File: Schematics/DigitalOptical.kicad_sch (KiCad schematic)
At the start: 112 parts, among them Q1 BSS138, Q2 BSS138, Q3 BSS138, Q4 BSS138, Q5 BSS138, Q6 BSS138, U100 PC817, U63 PC817, U64 PC817, U65 PCF8575, U66 PC817, U67 PC817, U68 PC817, U69 PC817, U70 PC817, U71 PC817, U72 PC817, U73 PC817, U74 LM1117-3.3, U75 PC817, U76 PC817, U77 PCF8575, U78 PCF8575, U79 PC817, U80 PC817, U81 PC817, U82 PC817, U83 PC817, U84 PC817, U85 PC817, U86 PC817, U87 LM1117-3.3, U88 LM1117-3.3, U89 PC817, U90 PC817, U91 PC817, U92 PC817, U93 PC817, U94 PC817, U95 PC817, U96 PC817, U97 PC817, U98 PC817, U99 PC817

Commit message: Prelude to split configurations.
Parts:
- removed C83, C84: .1µF, symbol Device:C_Small
- removed JD1, JD10, JD11, JD13, JD14, JD15, JD16, JD17, JD18, JD19, JD2, JD20, JD21, JD3, JD4, JD5, JD7, JD8: From 12v Analog, symbol Connector_Generic:Conn_01x02
- removed JD12, JD6, JD9: Conn_01x03, symbol Connector_keyed_kicad_sym:Conn_01x03
- removed Q1, Q2: BSS138, digikey-footprints:SOT-23-3, symbol dk_Transistors-FETs-MOSFETs-Single:BSS138
- removed U100, U63, U64, U66, U67, U68, U69, U70, U71, U72, U73, U75, U76, U79, U80, U81, U82, U83, U84, U85, U86, U89, U90, U91, U92, U93, U94, U95, U96, U97, U98, U99: PC817, Package_DIP:DIP-4_W7.62mm, symbol Isolator:PC817
- removed U65: PCF8575, IPC7351-Nominal:SOP65P775X200-24, symbol NXP:PCF8575
- removed U74: LM1117-3.3, symbol Regulator_Linear:LM1117-3.3
- added C20, C21: .1µF, symbol Device:C_Small
- added C30: 10µF, symbol Device:C_Polarized_Small_US
- added JP5: From 12v Analog, symbol Connector_Generic:Conn_01x02
- added Q13, Q14: BSS138, digikey-footprints:SOT-23-3, symbol dk_Transistors-FETs-MOSFETs-Single:BSS138
- added R153, R154, R155, R156, R157, R158, R159, R160, R161, R162, R163, R164, R165, R166: 10k, symbol Device:R_Small_US
- added U11: PCF8575, IPC7351-Nominal:SOP65P775X200-24, symbol NXP:PCF8575
- added U7: LM1117-3.3, symbol Regulator_Linear:LM1117-3.3
- R100, R101, R102, R103, R104, R107, R108, R111, R112, R113, R114, R115, R116, R117, R118, R119, R120, R121, R122, R123, R124, R85, R86, R87, R88, R91, R92, R93, R94, R97, R98, R99: value 220 -> 10k
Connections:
- net GNDA: now also C85.2, C86.2, C87.2, C88.2, JS3.3 (Pin_3), JS3.6 (Pin_6), U77.12 (VSS), U77.2 (A1), U77.21 (A0), U77.3 (A2), U78.12 (VSS), U78.2 (A1), U78.3 (A2), U87.1 (GND), U88.1 (GND), C30.2, JP5.2 (Pin_2)
- net SCL0: now also Q13.3; no longer R90.1
- net SDA0: now also Q14.3; no longer R95.1
- net at R120.2: now also C87.1, Q4.1, Q6.1, R106.2, R107.1, R108.2, R110.2, R111.1, R112.2, R113.1, R114.2, R115.1, R116.2, R117.1, R118.2, R119.1, R121.1, R122.2, R123.1, R124.2, U78.21 (A0), U78.24 (VDD), U88.2 (VO)
- net at R86.2: now also C86.1, Q3.1, Q5.1, R100.2, R105.2, R109.2, R85.1, R87.1, R88.2, R89.1, R90.2, R91.1, R92.2, R93.1, R94.2, R95.1, R96.2, R97.1, R98.2, R99.1, U77.24 (VDD), U87.2 (VO)
- net at R118.1: now also U78.16 (P13); no longer U78.17 (P14)
- net at U77.18 (P15): now also R90.1; no longer R119.2
- net at U77.9 (P05): now also R95.2; no longer R99.2
- net at R120.1: now also U78.15 (P12); no longer U78.18 (P15)
- net at R101.1: now also R102.2, R103.1, R104.2, C21.1, Q13.1, Q14.1, R153.2, R154.2, R155.1, R156.2, R157.1, R158.2, R159.1, R160.2, R161.1, R162.2, R163.1, R164.2, R165.1, R166.2, U11.2 (A1), U11.24 (VDD), U7.2 (VO)
- net at U78.10 (P06): now also R121.2; no longer R102.1
- net at R114.1: now also U78.18 (P15); no longer U78.15 (P12)
- net at U78.11 (P07): now also R123.2; no longer R104.1
- net at U78.9 (P05): now also R119.2; no longer R100.1
- net at U78.5 (P01): now also R111.2; no longer R88.1
- net at U77.14 (P11): now also R98.1; no longer R111.2
- net at R97.2: now also U77.10 (P06); no longer U77.8 (P04)
- net at R89.2: now also U77.6 (P02); no longer R96.2
- net at R96.1: now also U77.15 (P12)
- net at R113.2: now also U78.6 (P02); no longer U77.15 (P12)
- net at R107.2: now also U78.4 (P00); no longer U77.13 (P10)
- net at U77.7 (P03): now also R91.2; no longer R93.2
- net at R124.1: now also U78.13 (P10); no longer U78.20 (P17)
- net at R122.1: now also U78.14 (P11); no longer U78.19 (P16)
- net at R92.1: now also U77.17 (P14); no longer U78.6 (P02)
- net at R103.2: now also U11.5 (P01); no longer U77.11 (P07)
- net at R108.1: now also U78.20 (P17); no longer U78.13 (P10)
- net at R101.2: now also U11.4 (P00); no longer U77.10 (P06)
- net at U77.16 (P13): now also R94.1; no longer R115.2
- net at R117.2: now also U78.8 (P04); no longer U77.17 (P14)
- net at U77.19 (P16): now also R88.1; no longer R121.2
- net at U77.20 (P17): now also R86.1; no longer R123.2
- net at R112.1: now also U78.19 (P16); no longer U78.14 (P11)
- net at R116.1: now also U78.17 (P14); no longer U78.16 (P13)
- net at U78.7 (P03): now also R115.2; no longer R94.1
- net +5VD renamed +5V
- net +5V: now also C20.1, C30.1, JP5.1 (Pin_1), U7.3 (VI); no longer JS3.1 (Pin_1), JS3.2 (Pin_2), R90.2, R95.2
- new net: C20.2, C21.2, U11.12 (VSS), U11.21 (A0), U11.3 (A2), U7.1 (GND)
- new net: R157.2, U11.7 (P03)
- new net: R155.2, U11.6 (P02)
- new net: R164.1, U11.14 (P11)
- new net: Q14.2, R154.1, U11.23 (SDA)
- new net: R100.1, U77.13 (P10)
- new net: R159.2, U11.8 (P04)
- new net: R163.2, U11.10 (P06)
- new net: R165.2, U11.11 (P07)
- new net: R99.2, U77.11 (P07)
- new net: R93.2, U77.8 (P04)
- new net: Q13.2, R153.1, U11.22 (SCL)
- new net: R104.1, U11.19 (P16)
- new net: R162.1, U11.15 (P12)
- new net: R166.1, U11.13 (P10)
- new net: JS3.1 (Pin_1), JS3.2 (Pin_2)
- new net: R156.1, U11.18 (P15)
- new net: R161.2, U11.9 (P05)
- new net: R158.1, U11.17 (P14)
- new net: R160.1, U11.16 (P13)
- new net: R102.1, U11.20 (P17)
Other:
- moved on the sheet: C85, C86, C87, C88, JS3, Q3, Q4, Q5, Q6, R105, R106, R109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

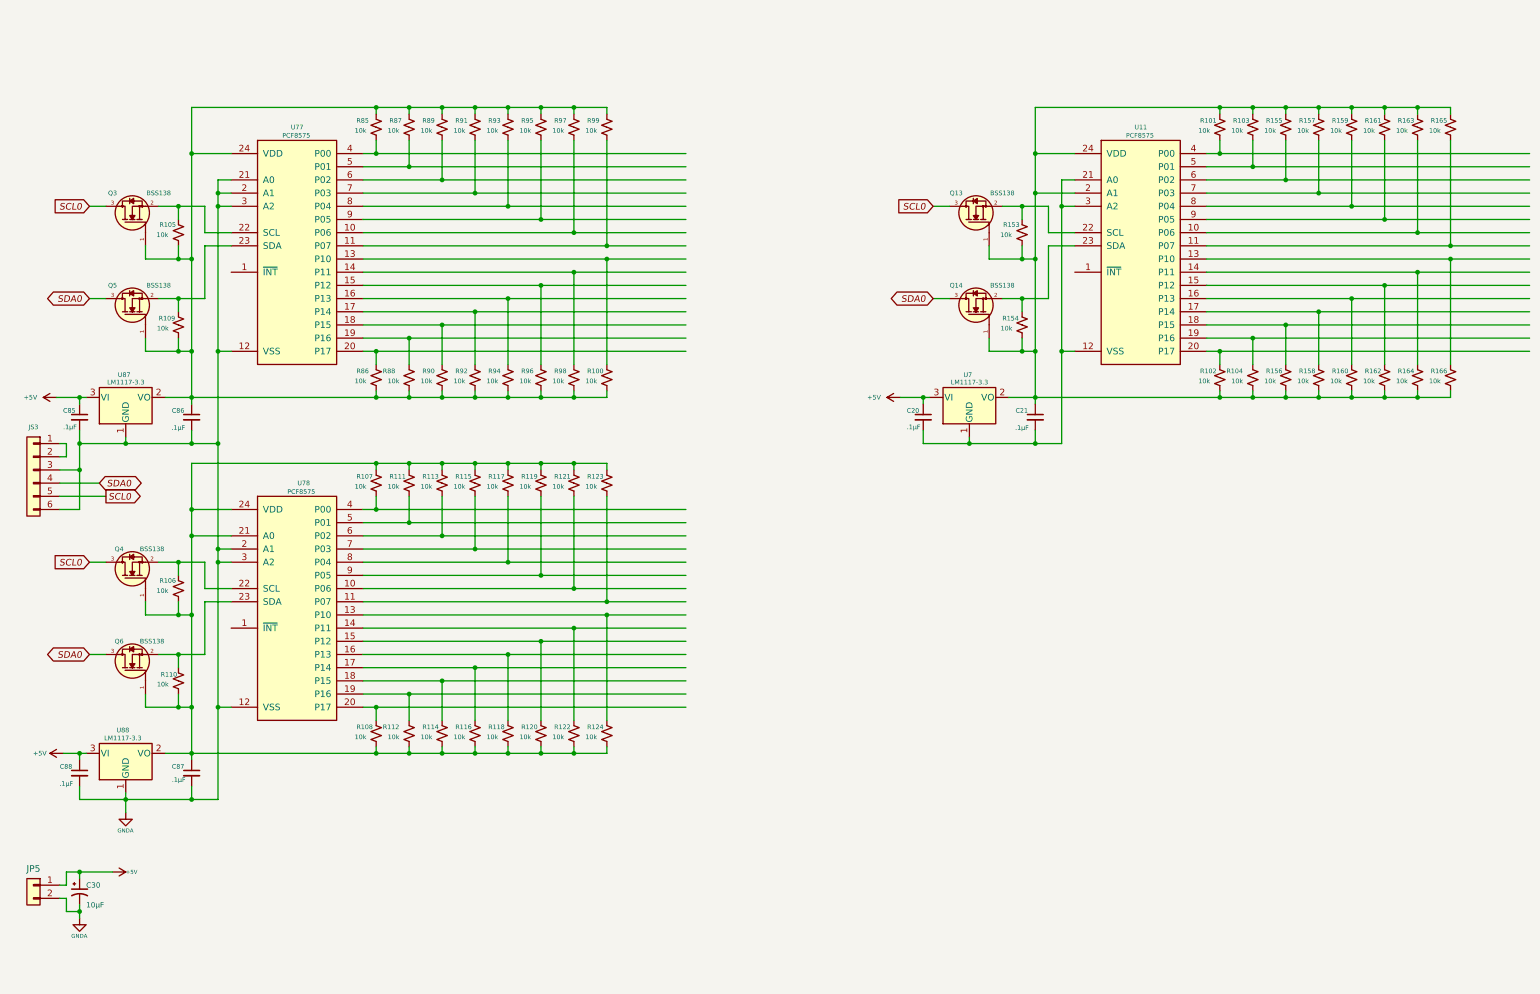
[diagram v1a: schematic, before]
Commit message: Upgreade byte value interface to short.  First stage of refactoring midi input for rotory encoders.  Still needs scaling.
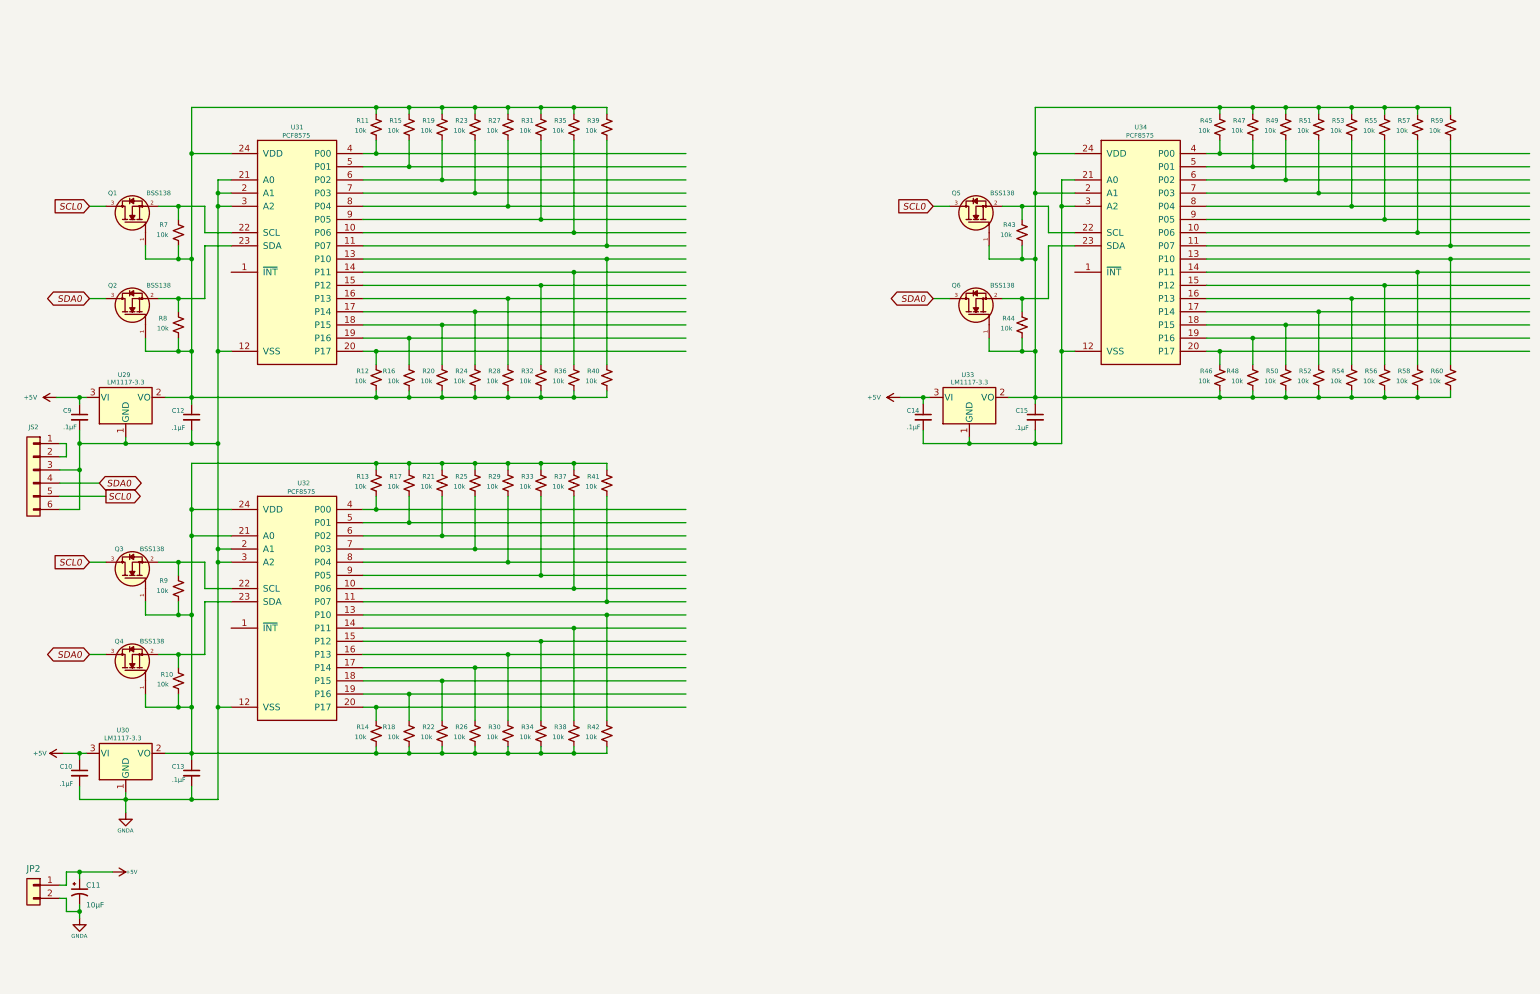
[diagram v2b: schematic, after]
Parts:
- renumbered C88 to C10, C30 to C11, C86 to C12, C87 to C13, C20 to C14, C21 to C15, C85 to C9, JP5 to JP2, JS3 to JS2, Q3 to Q1, Q5 to Q2, Q4 to Q3, Q6 to Q4, Q13 to Q5, Q14 to Q6, R110 to R10, R85 to R11, R86 to R12, R107 to R13, R108 to R14, R87 to R15, R88 to R16, R111 to R17, R112 to R18, R89 to R19, R90 to R20, R113 to R21, R114 to R22, R91 to R23, R92 to R24, R115 to R25, R116 to R26, R93 to R27, R94 to R28, R117 to R29, R118 to R30, R95 to R31, R96 to R32, R119 to R33, R120 to R34, R97 to R35, R98 to R36, R121 to R37, R122 to R38, R99 to R39, R100 to R40, R123 to R41, R124 to R42, R153 to R43, R154 to R44, R101 to R45, R102 to R46, R103 to R47, R104 to R48, R155 to R49, R156 to R50, R157 to R51, R158 to R52, R159 to R53, R160 to R54, R161 to R55, R162 to R56, R163 to R57, R164 to R58, R165 to R59, R166 to R60, R105 to R7, R109 to R8, R106 to R9, U87 to U29, U88 to U30, U77 to U31, U78 to U32, U7 to U33, U11 to U34

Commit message: Updated schematics including VCO and VCF daughter boards
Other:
- company:       MLE Tech                  Cedar Park, TX -> (none)
- title: Synth #2 -> Discrete Digital
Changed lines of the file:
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@@
 	(paper "USLegal")
 	(title_block
-		(title "Synth #2")
-		(date "2023-07-27")
-		(rev "0.1")
-		(company "      MLE Tech                  Cedar Park, TX")
-		(comment 2 "In Development")
+		(title "Discrete Digital")
+		(date "2025-01-16")
+		(rev "1.8")
+		(comment 1 "In Development ")
 	)
 	(junction

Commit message: Cleaned up page advance on display controls.
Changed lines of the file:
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@@
 (kicad_sch
-	(version 20231120)
+	(version 20250114)
 	(generator "eeschema")
-	(generator_version "8.0")
+	(generator_version "9.0")
 	(paper "USLegal")
 	(title_block
